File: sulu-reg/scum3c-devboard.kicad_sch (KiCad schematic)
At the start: 36 parts

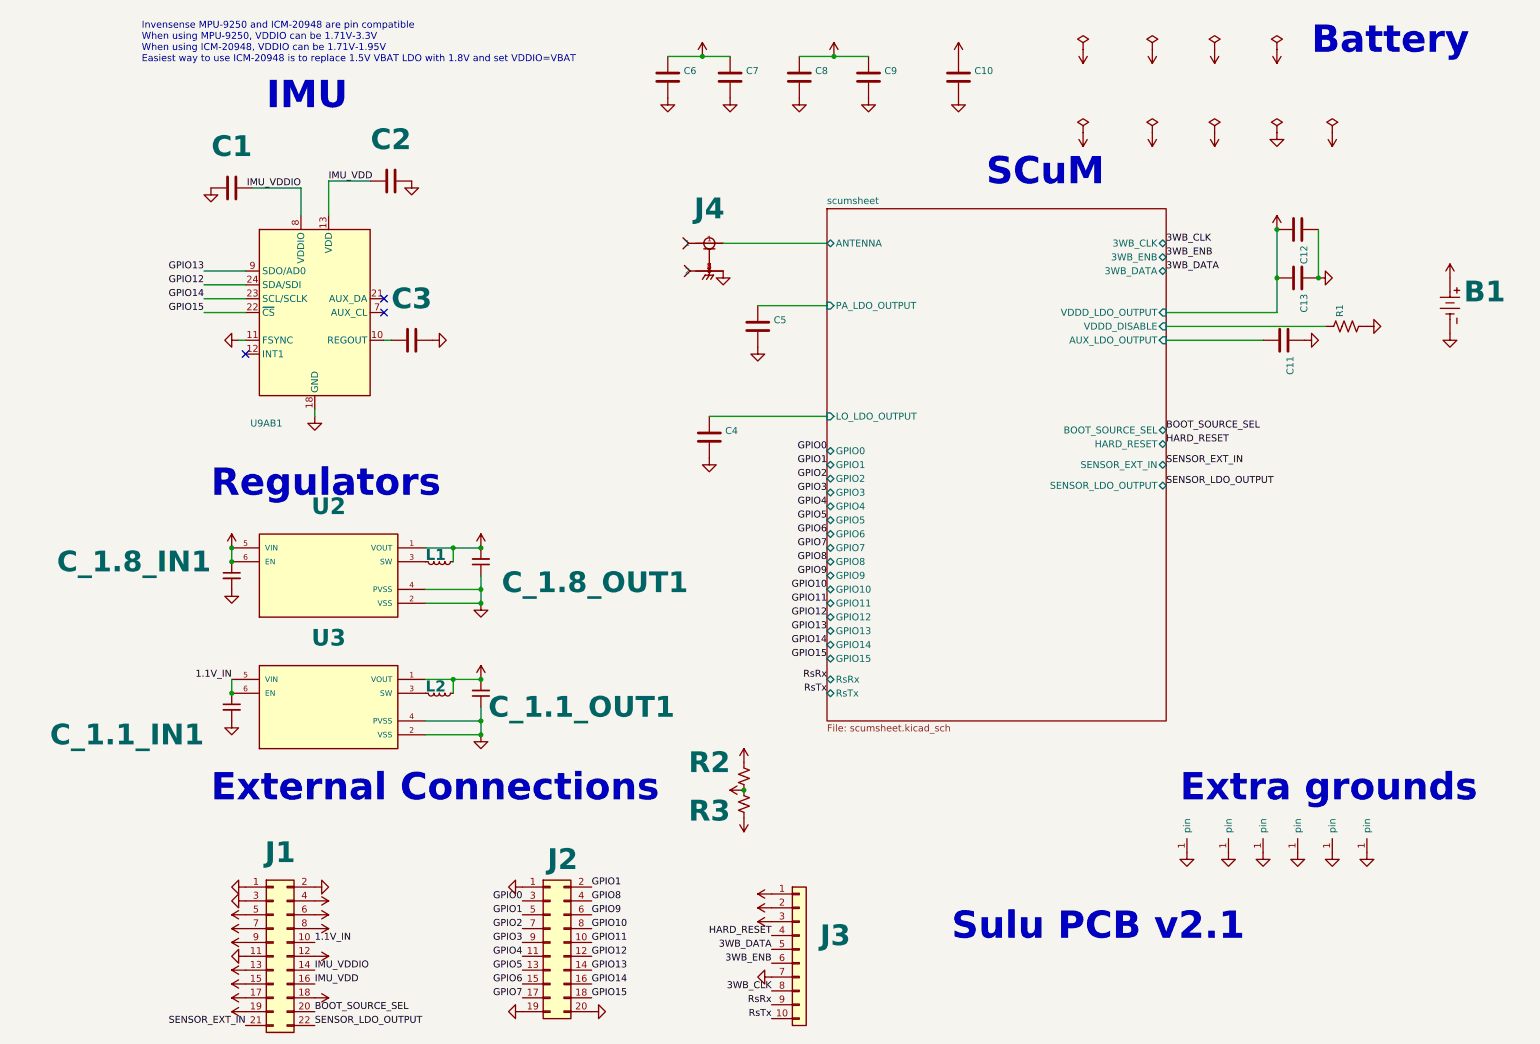
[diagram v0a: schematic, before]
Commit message: Re-order 3WB header locations
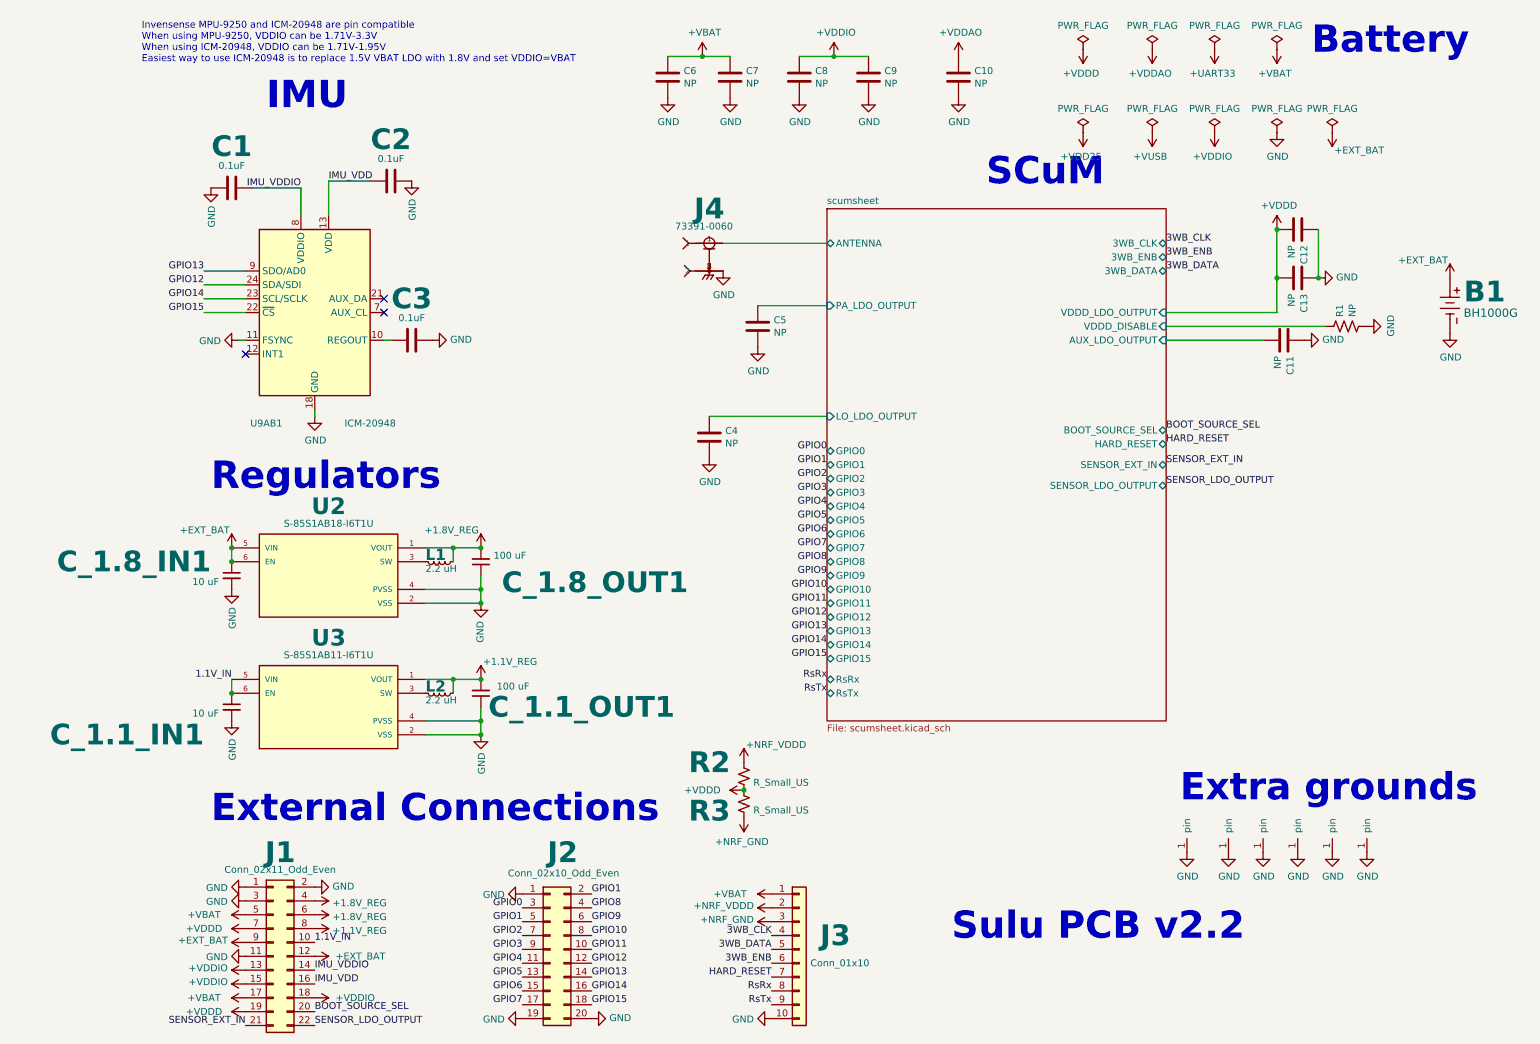
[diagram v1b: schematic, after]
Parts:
- B1: value (none) -> BH1000G; footprint (none) -> downloaded_libs:BH1000G
- C1, C2, C3: value (none) -> 0.1uF; footprint (none) -> Capacitor_SMD:C_0402_1005Metric
- C10, C11, C12, C13, C4, C5, C6, C7, C8, C9: value (none) -> NP; footprint (none) -> Capacitor_SMD:C_0402_1005Metric
- C_1.1_IN1, C_1.8_IN1: value (none) -> 10 uF; footprint (none) -> Capacitor_SMD:C_0402_1005Metric
- C_1.1_OUT1, C_1.8_OUT1: value (none) -> 100 uF; footprint (none) -> Capacitor_SMD:C_0402_1005Metric
- GND1, GND2, GND3, GND4, GND5, GND6: value (none) -> through_hole; footprint (none) -> SCUM:through_hole
- J1: value (none) -> Conn_02x11_Odd_Even; footprint (none) -> Connector_PinHeader_2.54mm:PinHeader_2x11_P2.54mm_Vertical
- J2: value (none) -> Conn_02x10_Odd_Even; footprint (none) -> Connector_PinHeader_2.54mm:PinHeader_2x10_P2.54mm_Vertical
- J3: value (none) -> Conn_01x10; footprint (none) -> Connector_PinHeader_2.54mm:PinHeader_1x10_P2.54mm_Vertical
- J4: value (none) -> 73391-0060; footprint (none) -> downloaded_libs:MOLEX_73391-0060
- L1, L2: value (none) -> 2.2 uH; footprint (none) -> Inductor_SMD:L_Wuerth_MAPI-2010
- R1: value (none) -> NP; footprint (none) -> Resistor_SMD:R_0402_1005Metric
- R2, R3: value (none) -> R_Small_US; footprint (none) -> Resistor_SMD:R_0402_1005Metric
- U2: value (none) -> S-85S1AB18-I6T1U; footprint (none) -> downloaded_libs:SOFL50P180X50-6N
- U3: value (none) -> S-85S1AB11-I6T1U; footprint (none) -> downloaded_libs:SOFL50P180X50-6N
- U9AB1: value (none) -> ICM-20948; footprint (none) -> Sensor_Motion:InvenSense_QFN-24_3x3mm_P0.4mm
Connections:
- net 3WB_CLK: now also J3.4 (Pin_4); no longer J3.8 (Pin_8)
- net GND: now also J3.10 (Pin_10); no longer J3.7 (Pin_7)
- net HARD_RESET: now also J3.7 (Pin_7); no longer J3.4 (Pin_4)
- net RsRx: now also J3.8 (Pin_8); no longer J3.9 (Pin_9)
- net RsTx: now also J3.9 (Pin_9); no longer J3.10 (Pin_10)
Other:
- note added: "Sulu PCB v2.2"
- note removed: "Sulu PCB v2.1"
- moved on the sheet: J2
